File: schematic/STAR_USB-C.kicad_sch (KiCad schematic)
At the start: 55 parts, among them J1 1017491, J2 1017491, J3 PD_DBG, J4 6120XX21621_61200621621, J5 Conn_01x02, J6 PD_I2C, J7 USB4216-03-A, U1 CAT24C512WI-GT3, U2 TPS25751DREFR, U3 TVS2200DRV

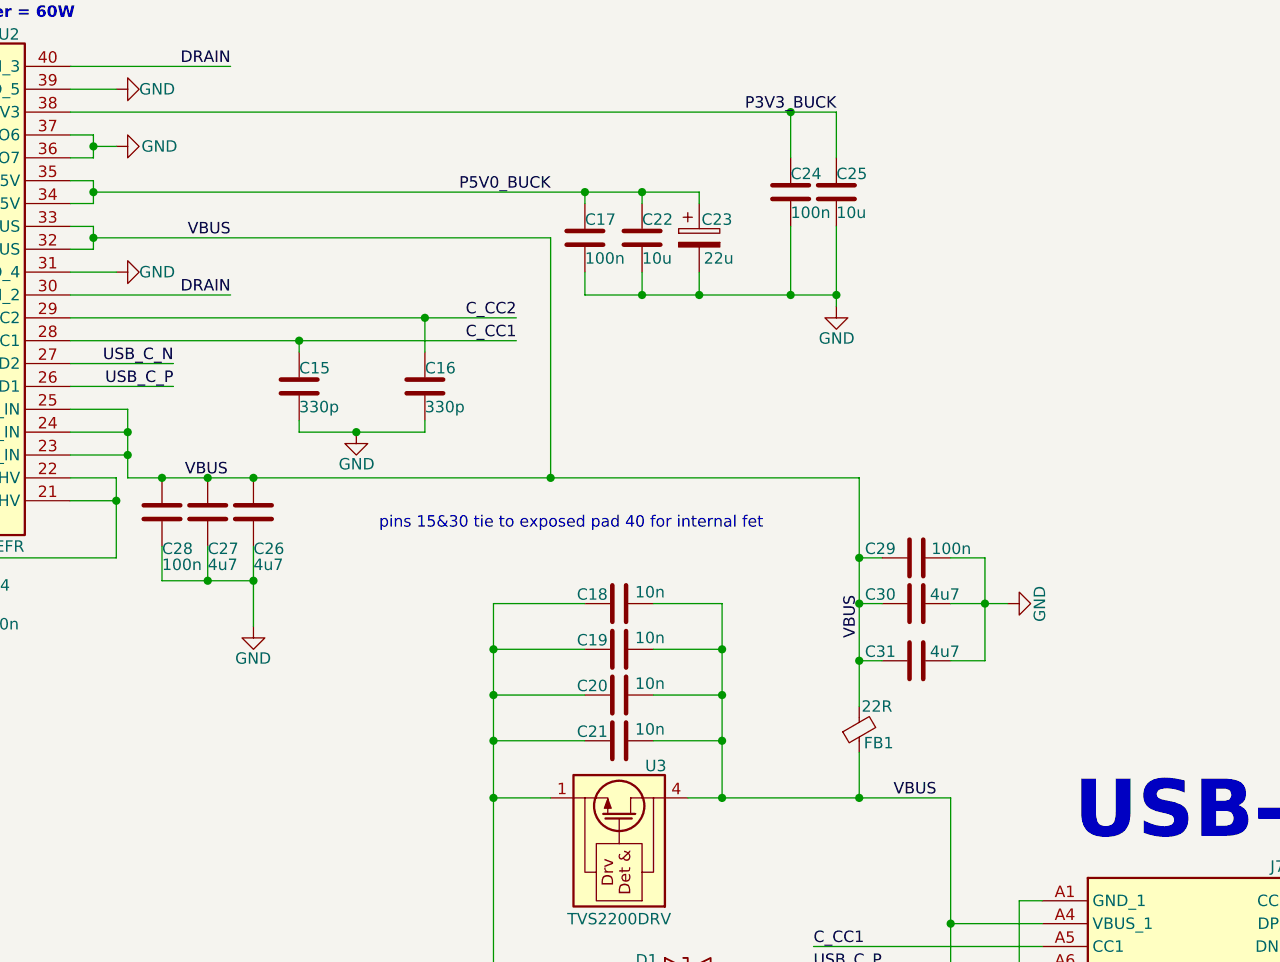
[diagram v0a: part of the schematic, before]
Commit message: fixed usb-c
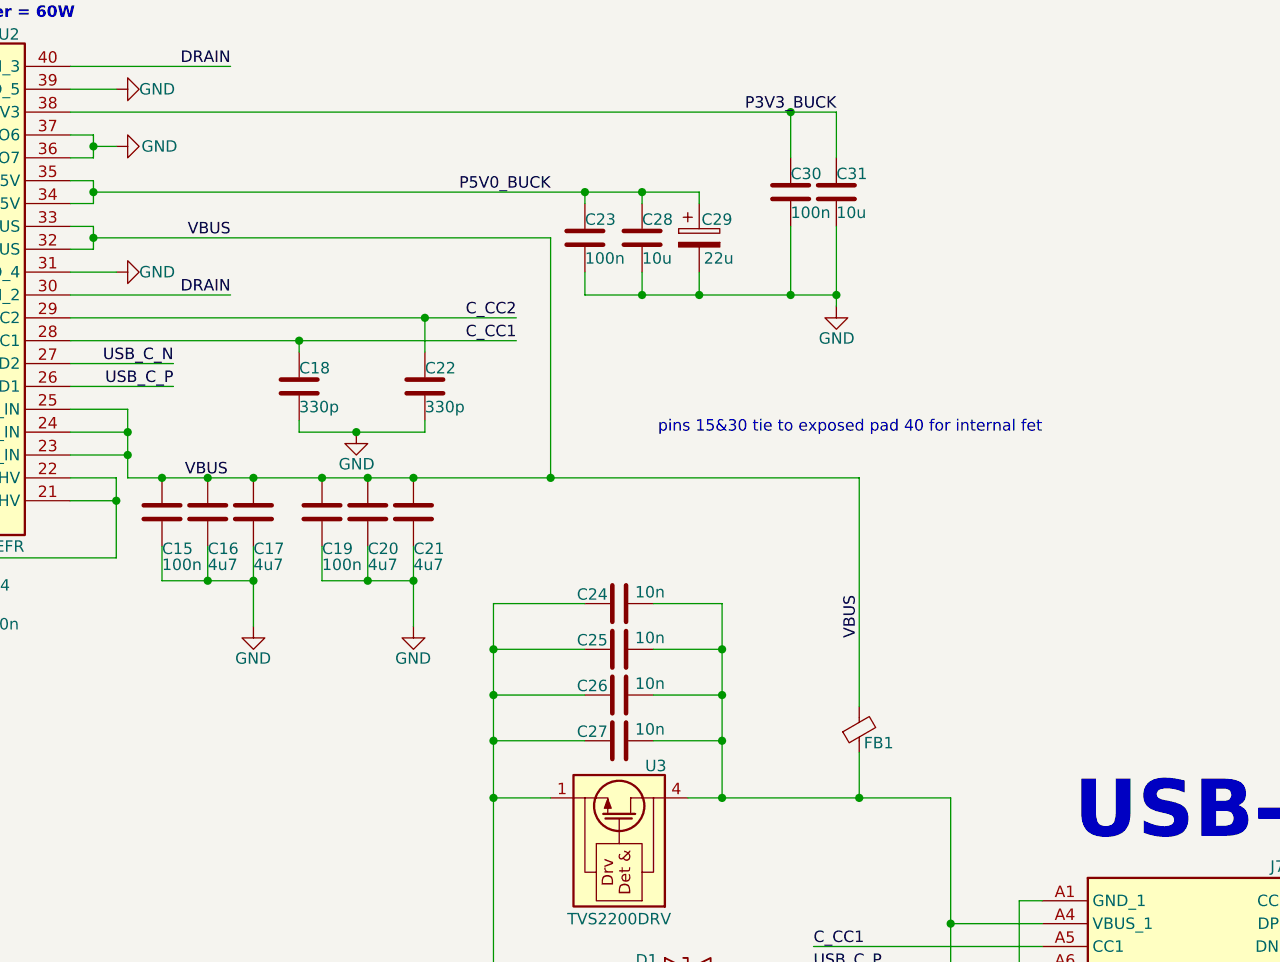
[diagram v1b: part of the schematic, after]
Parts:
- removed C29: 100n, Capacitor_SMD:C_0603_1608Metric_Pad1.08x0.95mm_HandSolder, symbol Device:C
- removed C30, C31: 4u7, Capacitor_SMD:C_0805_2012Metric_Pad1.18x1.45mm_HandSolder, symbol Device:C
- added C19: 100n, Capacitor_SMD:C_0603_1608Metric_Pad1.08x0.95mm_HandSolder, symbol Device:C
- added C20, C21: 4u7, Capacitor_SMD:C_0805_2012Metric_Pad1.18x1.45mm_HandSolder, symbol Device:C
- renumbered C28 to C15, C27 to C16, C26 to C17, C15 to C18, C16 to C22, C17 to C23, C18 to C24, C19 to C25, C20 to C26, C21 to C27, C22 to C28, C23 to C29, C24 to C30, C25 to C31
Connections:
- net GND: now also C19.2, C20.2, C21.2
- net VBUS: now also C19.1, C20.1, C21.1; no longer C24.2, C25.2, C26.2, C27.2, FB1.1, J7.A4 (VBUS_1), J7.B4 (VBUS_2), U3.4 (IN), U3.5 (IN), U3.6 (IN)
- new net: C24.2, C25.2, C26.2, C27.2, FB1.1, J7.A4 (VBUS_1), J7.B4 (VBUS_2), U3.4 (IN), U3.5 (IN), U3.6 (IN)

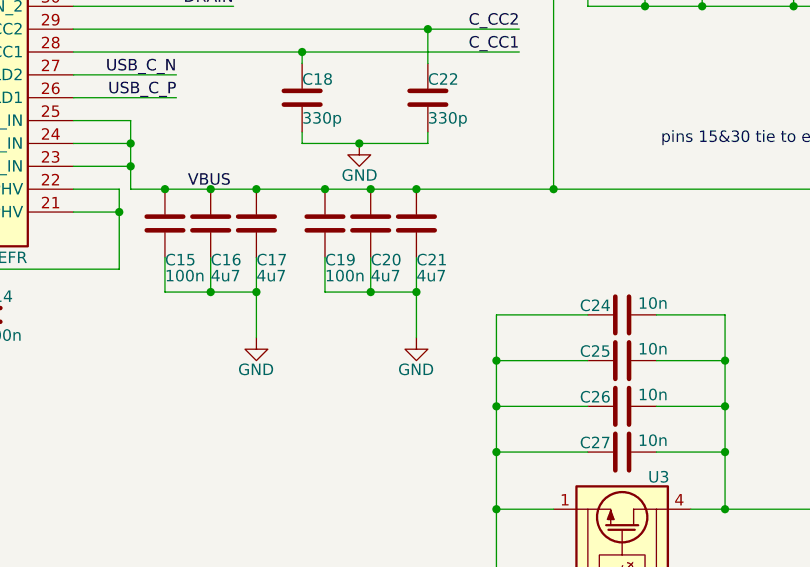
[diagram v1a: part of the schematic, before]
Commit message: fixed usb-c
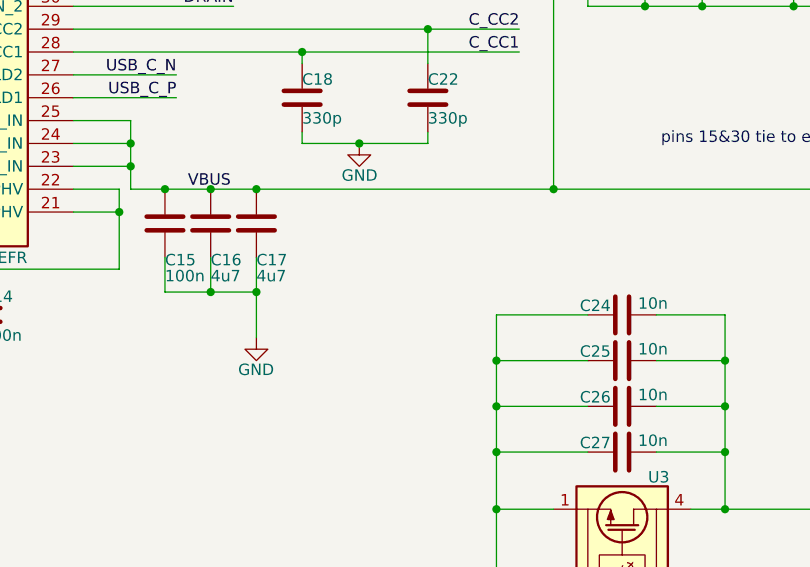
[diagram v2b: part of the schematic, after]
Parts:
- removed C19: 100n, Capacitor_SMD:C_0603_1608Metric_Pad1.08x0.95mm_HandSolder, symbol Device:C
- removed C20, C21: 4u7, Capacitor_SMD:C_0805_2012Metric_Pad1.18x1.45mm_HandSolder, symbol Device:C
